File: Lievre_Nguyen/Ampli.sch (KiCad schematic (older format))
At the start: 52 parts, among them J2 Conn_01x02, J3 Conn_01x03, Q1 2N2907, Q10 TIP32, Q11 BD138, Q12 TIP31, Q13 2N2222, Q2 2N2907, Q3 2N2907, Q4 2N2222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

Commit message: Fin de l'étape 'Saisie du schéma' - réalisation de l'empreinte du relay - numérotation des composants - vérifiaction ERC - association des empreintes - génération de la netlist
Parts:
- C1, C11, C3, C4, C5, C6, C7, C9: footprint (none) -> CmpAmpliAudio:CP_Radial_D8.0mm_P5.00mm
- C10, C8: footprint (none) -> CmpAmpliAudio:CP_Radial_D12.5mm_P5.00mm
- C2: footprint (none) -> CmpAmpliAudio:C_Rect_L7.2mm_W3.5mm_P5.00mm_FKS2_FKP2_MKS2_MKP2
- D1, D2: footprint Diode_THT:D_DO-35_SOD27_P7.62mm_Horizontal -> CmpAmpliAudio:D_DO-35_SOD27_P10.16mm_Horizontal
- Dz1: footprint (none) -> CmpAmpliAudio:D_DO-35_SOD27_P10.16mm_Horizontal
- Q1, Q13, Q2, Q3, Q4, Q5, Q6, Q7: footprint (none) -> CmpAmpliAudio:TO-18-3
- R1, R10, R13, R14, R15, R16, R17, R2, R3, R4, R5, R6, R7, R8, R9: footprint (none) -> CmpAmpliAudio:R_Axial_DIN0207_L6.3mm_D2.5mm_P10.16mm_Horizontal
- R11, R12: footprint (none) -> CmpAmpliAudio:R_Axial_DIN0516_L15.5mm_D5.0mm_P20.32mm_Horizontal
- RV1, RV2: footprint (none) -> CmpAmpliAudio:Potentiometer_Bourns_3296W_Vertical

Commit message: Fin du placement Plus de problème de relay
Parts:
- removed U1: Relay_1CT, Lievre_Nguyen:Relay_1CT, symbol Ampli-rescue:Relay_DIPxx-1Axx-11x-Ampli-cache
- added U1: Relay1_Relay_1CT, CmpAmpliAudio:Relais_112LMH2, symbol Ampli-rescue:Relay1_Relay_1CT-Ampli-cache
- C11, C5, C7, C9: footprint CmpAmpliAudio:CP_Radial_D8.0mm_P5.00mm -> CmpAmpliAudio:C_Rect_L7.2mm_W3.5mm_P5.00mm_FKS2_FKP2_MKS2_MKP2
- D1, D2: footprint CmpAmpliAudio:D_DO-35_SOD27_P10.16mm_Horizontal -> Diode_THT:D_DO-35_SOD27_P7.62mm_Horizontal
- Q10, Q12: footprint Package_TO_SOT_THT:TO-220-3_Vertical -> CmpAmpliAudio:TO-220-3_Vertical
- Q11, Q8, Q9: footprint Package_TO_SOT_THT:TO-126-3_Vertical -> CmpAmpliAudio:TO-126-3_Vertical
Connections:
- net +12V: now also U1.b2
- net at J2.1 (Pin_1): now also U1.c2
- net at D1.2 (A), Q13.3 (C): now also U1.b1
- net at R11.2, R12.1, R13.1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: now also U1.c1
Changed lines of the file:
@@
 encoding utf-8
 Sheet 1 1
-Title "Buck 45V vers 24/12V 13A"
-Date "2020-03-24"
-Rev "V0"
+Title "Ampli"
+Date "2020-04-10"
+Rev "V1"
 Comp "INSA GEI"
 Comment1 "AL"
@@
 F 0 "D1" H 8750 3916 50  0000 C CNN
 F 1 "1N4148" H 8750 3825 50  0000 C CNN
-F 2 "CmpAmpliAudio:D_DO-35_SOD27_P10.16mm_Horizontal" H 8750 3525 50  0001 C CNN
+F 2 "Diode_THT:D_DO-35_SOD27_P7.62mm_Horizontal" H 8750 3525 50  0001 C CNN
 F 3 "https://assets.nexperia.com/documents/data-sheet/1N4148_1N4448.pdf" H 8750 3700 50  0001 C CNN
 	1    8750 3700
@@
 F 0 "Q9" H 6292 2046 50  0000 L CNN
 F 1 "BD139" H 6292 1955 50  0000 L CNN
-F 2 "Package_TO_SOT_THT:TO-126-3_Vertical" H 6300 1925 50  0001 L CIN
+F 2 "CmpAmpliAudio:TO-126-3_Vertical" H 6300 1925 50  0001 L CIN
 F 3 "http://www.st.com/internet/com/TECHNICAL_RESOURCES/TECHNICAL_LITERATURE/DATASHEET/CD00001225.pdf" H 6100 2000 50  0001 L CNN
 	1    6100 2000
@@
 F 0 "C7" H 1815 6996 50  0000 L CNN
 F 1 "100n" H 1815 6905 50  0000 L CNN
-F 2 "CmpAmpliAudio:CP_Radial_D8.0mm_P5.00mm" H 1738 6800 50  0001 C CNN
+F 2 "CmpAmpliAudio:C_Rect_L7.2mm_W3.5mm_P5.00mm_FKS2_FKP2_MKS2_MKP2" H 1738 6800 50  0001 C CNN
 F 3 "~" H 1700 6950 50  0001 C CNN
 	1    1700 6950
@@
 F 0 "C5" H 1815 6346 50  0000 L CNN
 F 1 "100n" H 1815 6255 50  0000 L CNN
-F 2 "CmpAmpliAudio:CP_Radial_D8.0mm_P5.00mm" H 1738 6150 50  0001 C CNN
+F 2 "CmpAmpliAudio:C_Rect_L7.2mm_W3.5mm_P5.00mm_FKS2_FKP2_MKS2_MKP2" H 1738 6150 50  0001 C CNN
 F 3 "~" H 1700 6300 50  0001 C CNN
 	1    1700 6300
@@
 F 0 "Q8" H 5192 2546 50  0000 L CNN
 F 1 "BD139" H 5192 2455 50  0000 L CNN
-F 2 "Package_TO_SOT_THT:TO-126-3_Vertical" H 5200 2425 50  0001 L CIN
+F 2 "CmpAmpliAudio:TO-126-3_Vertical" H 5200 2425 50  0001 L CIN
 F 3 "http://www.st.com/internet/com/TECHNICAL_RESOURCES/TECHNICAL_LITERATURE/DATASHEET/CD00001225.pdf" H 5000 2500 50  0001 L CNN
 	1    5000 2500
@@
 F 0 "C9" H 7515 1496 50  0000 L CNN
 F 1 "100n" H 7515 1405 50  0000 L CNN
-F 2 "CmpAmpliAudio:CP_Radial_D8.0mm_P5.00mm" H 7438 1300 50  0001 C CNN
+F 2 "CmpAmpliAudio:C_Rect_L7.2mm_W3.5mm_P5.00mm_FKS2_FKP2_MKS2_MKP2" H 7438 1300 50  0001 C CNN
 F 3 "~" H 7400 1450 50  0001 C CNN
 	1    7400 1450
@@
 F 0 "Q11" H 6292 3696 50  0000 L CNN
 F 1 "BD138" H 6292 3605 50  0000 L CNN
-F 2 "Package_TO_SOT_THT:TO-126-3_Vertical" H 6300 3575 50  0001 L CIN
+F 2 "CmpAmpliAudio:TO-126-3_Vertical" H 6300 3575 50  0001 L CIN
 F 3 "http://www.st.com/internet/com/TECHNICAL_RESOURCES/TECHNICAL_LITERATURE/DATASHEET/CD00001225.pdf" H 6100 3650 50  0001 L CNN
 	1    6100 3650
@@
 F 0 "C11" H 7765 4296 50  0000 L CNN
 F 1 "100n" H 7765 4205 50  0000 L CNN
-F 2 "CmpAmpliAudio:CP_Radial_D8.0mm_P5.00mm" H 7688 4100 50  0001 C CNN
+F 2 "CmpAmpliAudio:C_Rect_L7.2mm_W3.5mm_P5.00mm_FKS2_FKP2_MKS2_MKP2" H 7688 4100 50  0001 C CNN
 F 3 "~" H 7650 4250 50  0001 C CNN
 	1    7650 4250
@@
 F 0 "D2" H 9850 4766 50  0000 C CNN
 F 1 "1N4148" H 9850 4675 50  0000 C CNN
-F 2 "CmpAmpliAudio:D_DO-35_SOD27_P10.16mm_Horizontal" H 9850 4375 50  0001 C CNN
+F 2 "Diode_THT:D_DO-35_SOD27_P7.62mm_Horizontal" H 9850 4375 50  0001 C CNN
 F 3 "https://assets.nexperia.com/documents/data-sheet/1N4148_1N4448.pdf" H 9850 4550 50  0001 C CNN
 	1    9850 4550
@@
 	8750 3250 8750 3550
 Wire Wire Line
-	9950 2850 10400 2850
-Wire Wire Line
-	9950 3250 10100 3250
-Wire Wire Line
 	8750 3850 9150 3850
 Wire Wire Line
@@
 F 0 "Q10" H 6741 1546 50  0000 L CNN
 F 1 "TIP32" H 6741 1455 50  0000 L CNN
-F 2 "Package_TO_SOT_THT:TO-220-3_Vertical" H 6800 1425 50  0001 L CIN
+F 2 "CmpAmpliAudio:TO-220-3_Vertical" H 6800 1425 50  0001 L CIN
 F 3 "https://www.centralsemi.com/get_document.php?cmp=1&mergetype=pd&mergepath=pd&pdf_id=tip41.PDF" H 6550 1500 50  0001 L CNN
 	1    6550 1500
@@
 F 0 "Q12" H 6741 4396 50  0000 L CNN
 F 1 "TIP31" H 6741 4305 50  0000 L CNN
-F 2 "Package_TO_SOT_THT:TO-220-3_Vertical" H 6800 4275 50  0001 L CIN
+F 2 "CmpAmpliAudio:TO-220-3_Vertical" H 6800 4275 50  0001 L CIN
 F 3 "https://www.centralsemi.com/get_document.php?cmp=1&mergetype=pd&mergepath=pd&pdf_id=tip41.PDF" H 6550 4350 50  0001 L CNN
 	1    6550 4350
@@
 Wire Wire Line
 	9150 3250 9350 3250
-$Comp
-L Ampli-rescue:Relay_DIPxx-1Axx-11x-Ampli-cache U1
-U 1 1 5E6CB02F
-P 9650 3050
-F 0 "U1" V 10117 3050 50  0000 C CNN
-F 1 "Relay_1CT" V 10026 3050 50  0000 C CNN
-F 2 "Lievre_Nguyen:Relay_1CT" H 10000 3000 50  0001 L CNN
-F 3 "" H 9650 3050 50  0001 C CNN
-	1    9650 3050
-	0    -1   -1   0
-$EndComp
 $Comp
 L Ampli-rescue:Device_D_Zener_ALT-Ampli-cache Dz1
@@
 Wire Wire Line
 	1700 3900 1700 4150
+Wire Wire Line
+	9950 2850 10400 2850
+Wire Wire Line
+	9950 3250 10100 3250
+$Comp
+L Ampli-rescue:Relay1_Relay_1CT-Ampli-cache U1
+U 1 1 5E9F58B6
+P 9300 3050
+F 0 "U1" V 9767 2700 50  0000 C CNN
+F 1 "Relay1_Relay_1CT" V 9676 2700 50  0000 C CNN
+F 2 "CmpAmpliAudio:Relais_112LMH2" H 9300 3050 50  0001 C CNN
+F 3 "" H 9300 3050 50  0001 C CNN
+	1    9300 3050
+	0    -1   -1   0
+$EndComp
 $EndSCHEMATC

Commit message: Fin du routage
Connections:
- net -12V: no longer Q2.2 (B), R14.1, R15.1
- net GND: now also C5.2, C7.1, J3.2 (Pin_2)
- net at R9.2: no longer Q7.1 (E)
- net at Q6.1 (E): no longer R7.2
- new net: Q2.2 (B), R14.1, R15.1
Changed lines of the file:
@@
 	2150 6050 2150 6150
-Wire Wire Line
-	1750 6700 2150 6700
 Wire Wire Line
 	2150 6700 2150 6800
@@
 Wire Wire Line
 	2350 5000 3250 5000
-Wire Wire Line
-	3250 5000 3750 5000
 Connection ~ 3250 5000
 Connection ~ 2350 3850
@@
 	3900 1000 3900 1100
 Connection ~ 3650 1000
-Wire Wire Line
-	3900 1400 3900 1500
 $Comp
 L Device:Q_PNP_EBC Q6
@@
 	-1   0    0    -1
 $EndComp
-Connection ~ 3900 1500
-Wire Wire Line
-	3900 1500 3900 1650
-Wire Wire Line
-	5100 1500 5100 1650
 Wire Wire Line
 	2350 3050 2800 3050
@@
 Wire Wire Line
 	3550 3400 3750 3400
-Wire Wire Line
-	3750 5000 4000 5000
 Wire Wire Line
 	4000 5000 4000 5250
@@
 	1    0    0    1
 $EndComp
-Connection ~ 5100 1500
-Wire Wire Line
-	5100 1400 5100 1500
 $Comp
 L Device:R R7
@@
 	1    0    0    -1
 $EndComp
-Connection ~ 3750 5000
-Wire Wire Line
-	3750 5000 3750 5600
-Wire Wire Line
-	3750 3400 3750 5000
 Wire Wire Line
 	3250 4400 3250 5000
@@
 	2350 4400 2350 5000
 Wire Wire Line
-	4000 5000 5100 5000
-Wire Wire Line
 	5100 5000 5100 4800
-Connection ~ 4000 5000
 Wire Wire Line
 	5100 4400 5100 4500
@@
 Wire Wire Line
 	5100 5000 6650 5000
-Connection ~ 5100 5000
 Wire Wire Line
 	7650 4650 7650 4400
@@
 	0    -1   -1   0
 $EndComp
+Connection ~ 5100 5000
+Connection ~ 4000 5000
+Wire Wire Line
+	4000 5000 5100 5000
+Wire Wire Line
+	3250 5000 4000 5000
+Wire Wire Line
+	3750 3400 3750 5600
+Wire Wire Line
+	3900 1400 3900 1650
+Wire Wire Line
+	5100 1400 5100 1650
+Wire Wire Line
+	1700 6700 2150 6700
 $EndSCHEMATC

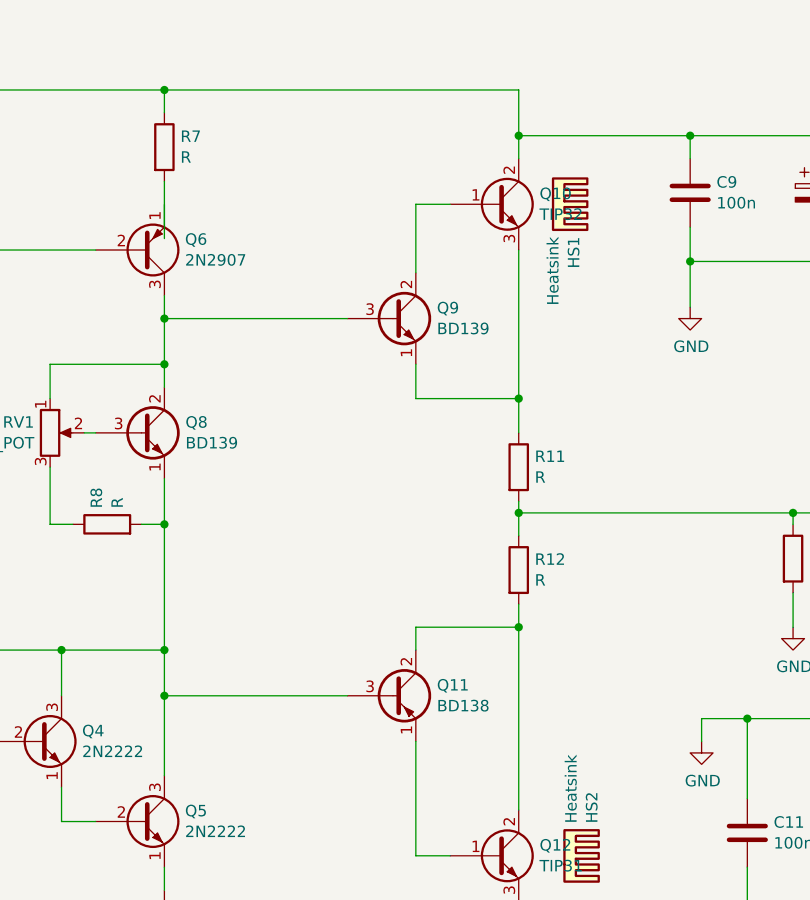
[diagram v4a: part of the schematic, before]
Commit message: Fin du routage Résolution de quelques petites erreurs
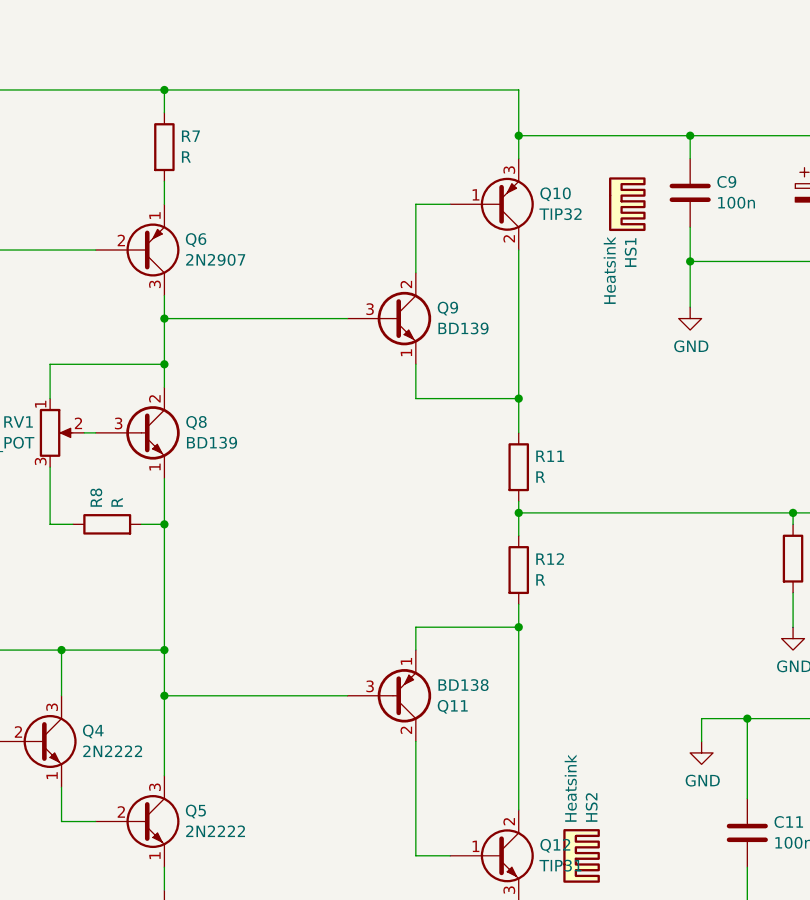
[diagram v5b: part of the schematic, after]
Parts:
- removed Q10: TIP32, CmpAmpliAudio:TO-220-3_Vertical, symbol Transistor_BJT:TIP41
- added Q10: TIP32, CmpAmpliAudio:TO-220-3_Vertical, symbol Transistor_BJT:TIP42
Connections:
- net +12V: now also Q10.3 (E)
- net at Q9.1 (E), R11.1: now also Q10.2 (C)
- net at Q9.2 (C): now also Q10.1 (B)
- net at Q6.1 (E): now also R7.2
- net at Q12.2 (C), R12.2: now also Q11.1 (E); no longer Q11.2 (C)
- net at Q12.1 (B): now also Q11.2 (C); no longer Q11.1 (E)
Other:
- moved on the sheet: HS1
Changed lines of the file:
@@
 L Mechanical:Heatsink HS1
 U 1 1 5E6AD543
-P 6800 1500
-F 0 "HS1" H 6942 1621 50  0000 L TNN
-F 1 "Heatsink" H 6942 1530 50  0000 L TNN
-F 2 "CmpAmpliAudio:Heatsink_Fischer_SK104-STC-STIC_35x13mm_2xDrill2.5mm" H 6812 1500 50  0001 C CNN
-F 3 "~" H 6812 1500 50  0001 C CNN
-	1    6800 1500
+P 7050 1500
+F 0 "HS1" H 7192 1621 50  0000 L TNN
+F 1 "Heatsink" H 7192 1530 50  0000 L TNN
+F 2 "CmpAmpliAudio:Heatsink_Fischer_SK104-STC-STIC_35x13mm_2xDrill2.5mm" H 7062 1500 50  0001 C CNN
+F 3 "~" H 7062 1500 50  0001 C CNN
+	1    7050 1500
 	0    1    1    0
 $EndComp
@@
 F 3 "http://www.st.com/internet/com/TECHNICAL_RESOURCES/TECHNICAL_LITERATURE/DATASHEET/CD00001225.pdf" H 6100 3650 50  0001 L CNN
 	1    6100 3650
-	1    0    0    -1
+	1    0    0    1
 $EndComp
 $Comp
@@
 	1    0    0    -1
 $EndComp
-$Comp
-L Transistor_BJT:TIP41 Q10
-U 1 1 5E6B88C4
-P 6550 1500
-F 0 "Q10" H 6741 1546 50  0000 L CNN
-F 1 "TIP32" H 6741 1455 50  0000 L CNN
-F 2 "CmpAmpliAudio:TO-220-3_Vertical" H 6800 1425 50  0001 L CIN
-F 3 "https://www.centralsemi.com/get_document.php?cmp=1&mergetype=pd&mergepath=pd&pdf_id=tip41.PDF" H 6550 1500 50  0001 L CNN
-	1    6550 1500
-	1    0    0    -1
-$EndComp
 Wire Wire Line
 	6650 1200 6650 1300
@@
 	3900 1400 3900 1650
 Wire Wire Line
-	5100 1400 5100 1650
+	5100 1400 5100 1500
 Wire Wire Line
 	1700 6700 2150 6700
+$Comp
+L Transistor_BJT:TIP42 Q10
+U 1 1 5EAA567E
+P 6550 1500
+F 0 "Q10" H 6741 1454 50  0000 L CNN
+F 1 "TIP32" H 6741 1545 50  0000 L CNN
+F 2 "CmpAmpliAudio:TO-220-3_Vertical" H 6800 1425 50  0001 L CIN
+F 3 "https://www.centralsemi.com/get_document.php?cmp=1&mergetype=pd&mergepath=pd&pdf_id=TIP42.PDF" H 6550 1500 50  0001 L CNN
+	1    6550 1500
+	1    0    0    1
+$EndComp
 $EndSCHEMATC

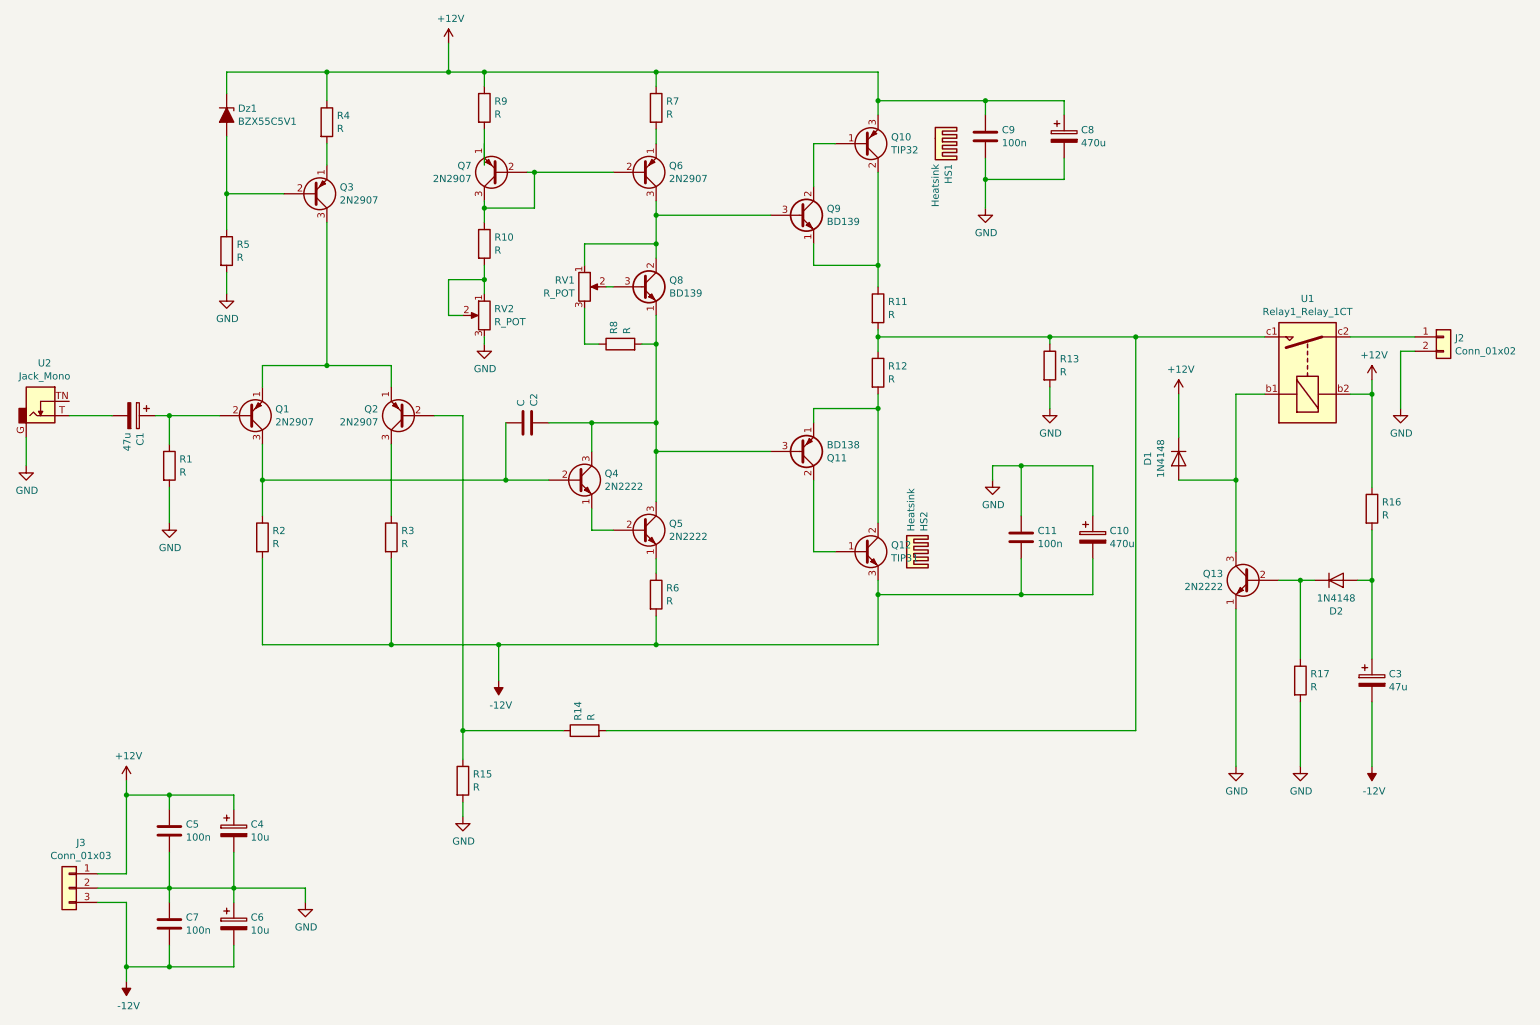
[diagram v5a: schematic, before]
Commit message: Correction des erreurs sauf erreur 'bornier d'enceinte (sortie)'
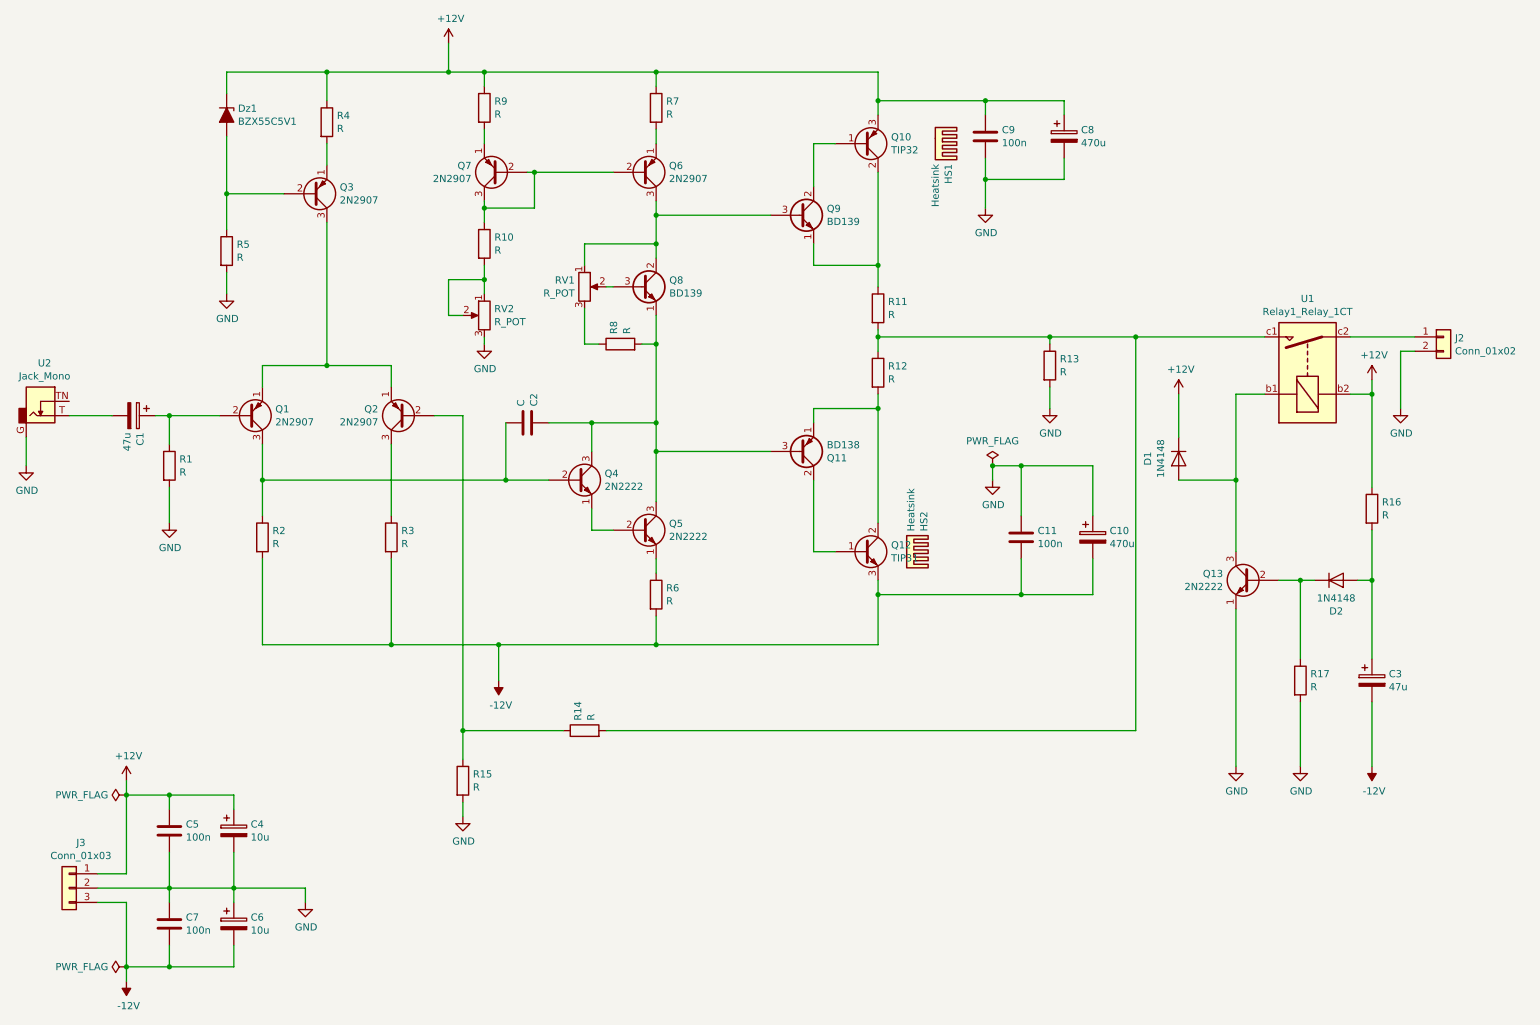
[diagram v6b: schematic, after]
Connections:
- net at R9.2: now also Q7.1 (E)
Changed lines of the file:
@@
 	3750 3400 3750 5600
-Wire Wire Line
-	3900 1400 3900 1650
 Wire Wire Line
 	5100 1400 5100 1500
@@
 	1    0    0    1
 $EndComp
+Wire Wire Line
+	3900 1400 3900 1500
+$Comp
+L power:PWR_FLAG #FLG0101
+U 1 1 5EBE207B
+P 7450 3750
+F 0 "#FLG0101" H 7450 3825 50  0001 C CNN
+F 1 "PWR_FLAG" H 7450 3923 50  0000 C CNN
+F 2 "" H 7450 3750 50  0001 C CNN
+F 3 "~" H 7450 3750 50  0001 C CNN
+	1    7450 3750
+	1    0    0    -1
+$EndComp
+Connection ~ 7450 3750
+$Comp
+L power:PWR_FLAG #FLG0102
+U 1 1 5EBEF198
+P 1400 7250
+F 0 "#FLG0102" H 1400 7325 50  0001 C CNN
+F 1 "PWR_FLAG" V 1400 7377 50  0000 L CNN
+F 2 "" H 1400 7250 50  0001 C CNN
+F 3 "~" H 1400 7250 50  0001 C CNN
+	1    1400 7250
+	0    -1   -1   0
+$EndComp
+$Comp
+L power:PWR_FLAG #FLG?
+U 1 1 5EBF02A2
+P 1400 6050
+F 0 "#FLG?" H 1400 6125 50  0001 C CNN
+F 1 "PWR_FLAG" V 1400 6177 50  0000 L CNN
+F 2 "" H 1400 6050 50  0001 C CNN
+F 3 "~" H 1400 6050 50  0001 C CNN
+	1    1400 6050
+	0    -1   -1   0
+$EndComp
 $EndSCHEMATC
